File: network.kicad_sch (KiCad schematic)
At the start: 66 parts, among them J1 1840888-1, Q1 BSS138, Q2 BSS138, Q3 BSS138, U2 DP83867IRPAPR, Y1 ECS-2520MV-xxx-xx

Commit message: MDIX routing done
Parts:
- removed TP3: TestPoint, TestPoint:TestPoint_Pad_1.0x1.0mm, symbol Connector:TestPoint
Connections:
- net MD0_P: now reaches J1.2 (MD0+), U2.2 (TD_P_A)
- net MD0_N: now reaches J1.3 (MD0-), U2.3 (TD_M_A)
- net MD1_P: now reaches J1.4 (MD1+), U2.5 (TD_P_B)
- net MD1_N: now reaches J1.5 (MD1-), U2.6 (TD_M_B)
- net MD2_P: now reaches J1.6 (MD2+), U2.10 (TD_P_C)
- net MD2_N: now reaches J1.7 (MD2-), U2.11 (TD_M_C)
- net MD3_P: now reaches J1.8 (MD3+), U2.13 (TD_P_D)
- net MD3_N: now reaches J1.9 (MD3-), U2.14 (TD_M_D)
- no-connect marks 21 -> 22
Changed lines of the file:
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@@
+	)
+	(no_connect
+		(at 200.66 35.56)
 	)
 	(no_connect
@@
 		)
 	)
+	(label "MD2_P"
+		(at 218.44 58.42 0)
+		(effects
+			(font
+				(size 1.27 1.27)
+			)
+			(justify left bottom)
+		)
+	)
+	(label "MD2_N"
+		(at 218.44 60.96 0)
+		(effects
+			(font
+				(size 1.27 1.27)
+			)
+			(justify left bottom)
+		)
+	)
 	(label "LED2"
 		(at 262.89 148.59 180)
@@
 		)
 	)
+	(label "MD0_P"
+		(at 218.44 43.18 0)
+		(effects
+			(font
+				(size 1.27 1.27)
+			)
+			(justify left bottom)
+		)
+	)
 	(label "LED1"
 		(at 236.22 148.59 180)
@@
 		)
 	)
+	(label "MD0_N"
+		(at 218.44 45.72 0)
+		(effects
+			(font
+				(size 1.27 1.27)
+			)
+			(justify left bottom)
+		)
+	)
 	(label "3V3"
 		(at 20.32 106.68 180)
@@
 		)
 	)
+	(label "MD3_N"
+		(at 218.44 68.58 0)
+		(effects
+			(font
+				(size 1.27 1.27)
+			)
+			(justify left bottom)
+		)
+	)
 	(label "X_IN"
 		(at 198.12 121.92 0)
@@
 		)
 	)
+	(label "MD3_P"
+		(at 218.44 66.04 0)
+		(effects
+			(font
+				(size 1.27 1.27)
+			)
+			(justify left bottom)
+		)
+	)
 	(label "3V3"
 		(at 124.46 22.86 0)
+		(effects
+			(font
+				(size 1.27 1.27)
+			)
+			(justify left bottom)
+		)
+	)
+	(label "MD1_N"
+		(at 218.44 53.34 0)
+		(effects
+			(font
+				(size 1.27 1.27)
+			)
+			(justify left bottom)
+		)
+	)
+	(label "MD1_P"
+		(at 218.44 50.8 0)
 		(effects
 			(font
@@
 		(length 2.54)
 		(shape round)
-		(at 222.25 68.58 180)
-		(fields_autoplaced yes)
-		(effects
-			(font
-				(size 1.27 1.27)
-			)
-			(justify right bottom)
-		)
-		(property "Netclass" "MDI_DIFF_PAIR"
-			(at 222.9485 71.12 0)
-			(effects
-				(font
-					(size 1.27 1.27)
-				)
-				(justify left)
-			)
-		)
-		(property "Component Class" ""
-			(at -152.4 -1.27 0)
-			(effects
-				(font
-					(size 1.27 1.27)
-					(italic yes)
-				)
-			)
-		)
-	)
-	(netclass_flag ""
-		(length 2.54)
-		(shape round)
 		(at 101.6 83.82 180)
 		(fields_autoplaced yes)
@@
 				)
 			)
-		)
-	)
-	(symbol
-		(lib_id "Connector:TestPoint")
-		(at 200.66 35.56 270)
-		(unit 1)
-		(exclude_from_sim no)
-		(in_bom yes)
-		(on_board yes)
-		(dnp no)
-		(fields_autoplaced yes)
-		(property "Reference" "TP3"
-			(at 205.74 34.2899 90)
-			(effects
-				(font
-					(size 1.27 1.27)
-				)
-				(justify left)
-			)
-		)
-		(property "Value" "TestPoint"
-			(at 205.74 36.8299 90)
-			(effects
-				(font
-					(size 1.27 1.27)
-				)
-				(justify left)
-			)
-		)
-		(property "Footprint" "TestPoint:TestPoint_Pad_1.0x1.0mm"
-			(at 200.66 40.64 0)
-			(effects
-				(font
-					(size 1.27 1.27)
-				)
-				(hide yes)
-			)
-		)
-		(property "Datasheet" "~"
-			(at 200.66 40.64 0)
-			(effects
-				(font
-					(size 1.27 1.27)
-				)
-				(hide yes)
-			)
-		)
-		(property "Description" "test point"
-			(at 200.66 35.56 0)
-			(effects
-				(font
-					(size 1.27 1.27)
-				)
-				(hide yes)
-			)
-		)
-		(pin "1"
-		)
-		(instances
-			(project "pocketbeagle2 revA_241205"
-				(path "/82320ebb-b624-4fc9-8d5a-3bc164182d09/1a5f5f50-6711-4dc3-8e4f-1634784841ca"
-					(reference "TP3")
-					(unit 1)
-				)
-			)

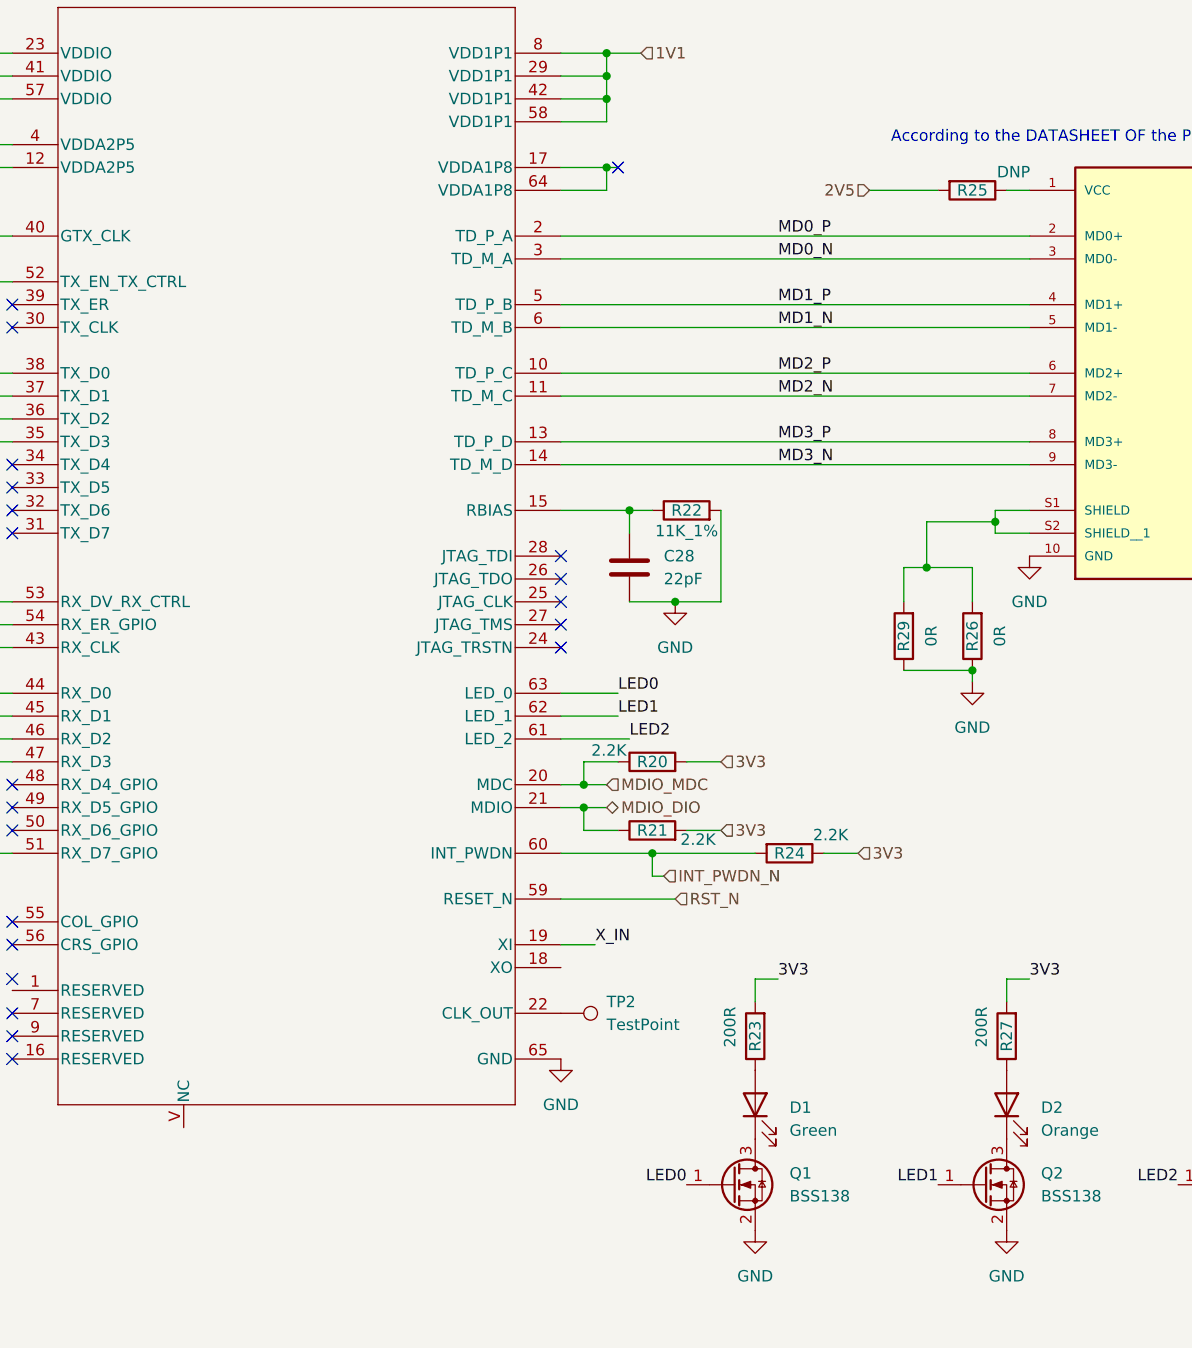
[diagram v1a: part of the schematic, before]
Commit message: Fully routed PCB, missing fligth time matching on the RGMII
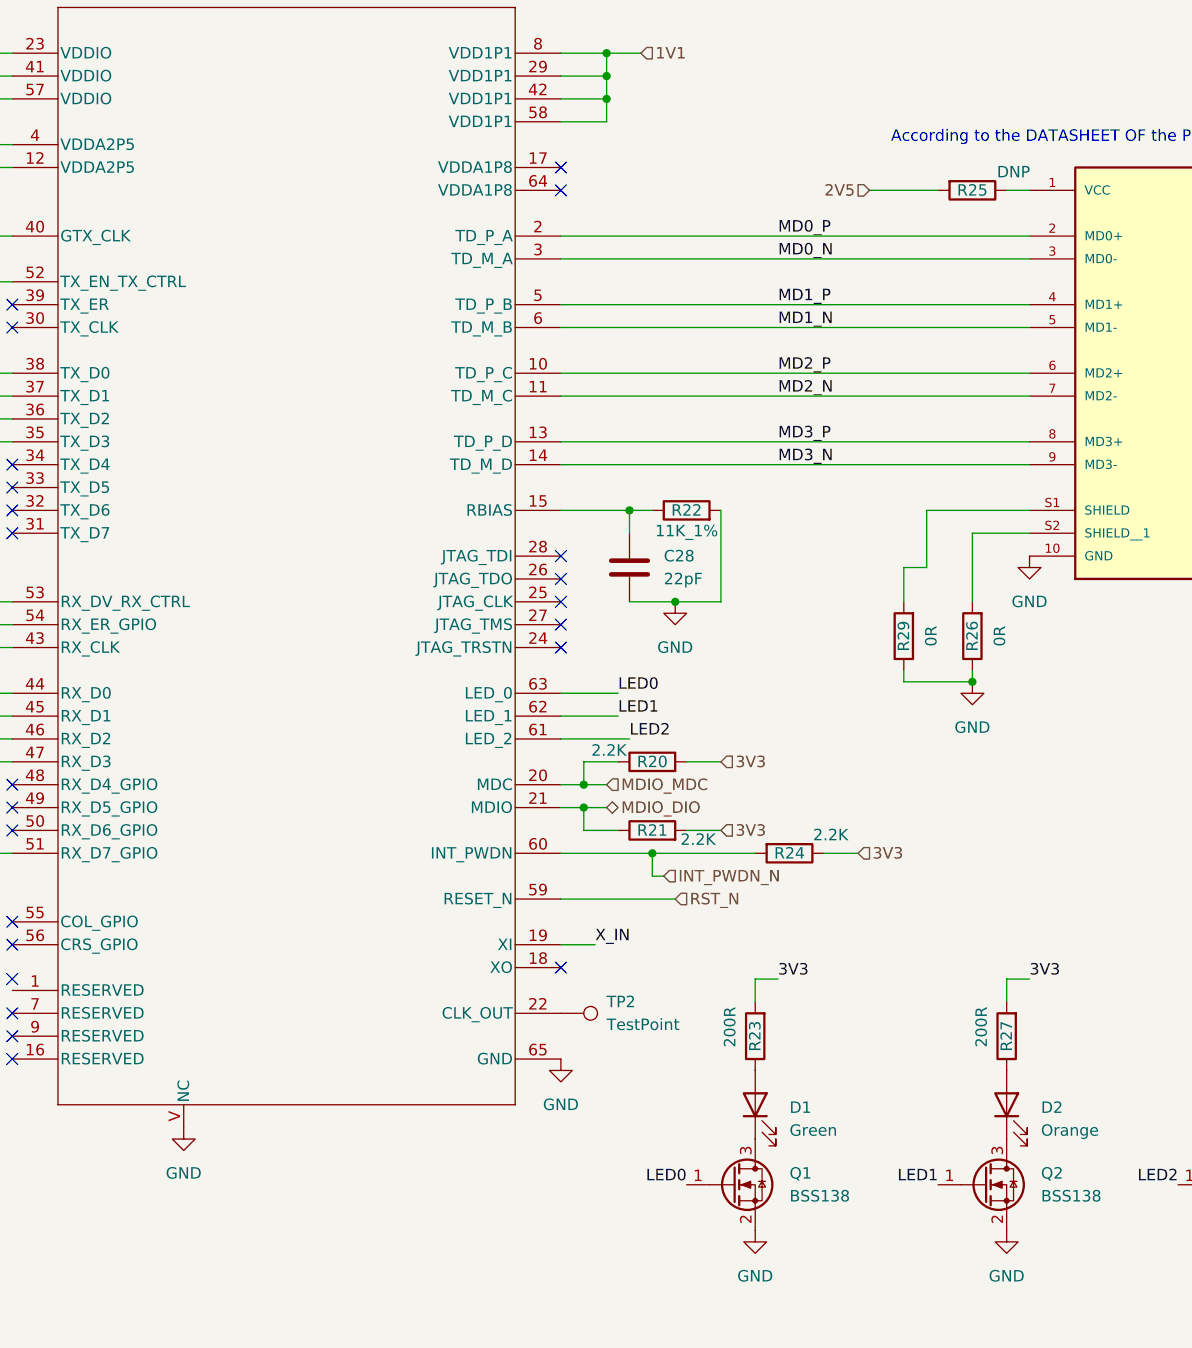
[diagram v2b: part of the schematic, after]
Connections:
- net GND: now also U2.V (NC)
- net at J1.S2 (SHIELD__1), R26.2: no longer J1.S1 (SHIELD), R29.2
- net at U2.17 (VDDA1P8): no longer U2.64 (VDDA1P8)
- new net: J1.S1 (SHIELD), R29.2
- no-connect marks 22 -> 24
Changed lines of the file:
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@@
 	)
 	(junction
+		(at 240.03 92.71)
+		(diameter 0)
+		(color 0 0 0 0)
+	)
+	(junction
 		(at 72.39 177.8)
 		(diameter 0)
@@
 	)
 	(junction
-		(at 240.03 91.44)
-		(diameter 0)
-		(color 0 0 0 0)
-	)
-	(junction
 		(at 110.49 171.45)
 		(diameter 0)
@@
 	)
 	(junction
-		(at 234.95 80.01)
-		(diameter 0)
-		(color 0 0 0 0)
-	)
-	(junction
 		(at 85.09 163.83)
 		(diameter 0)
@@
 	)
 	(junction
-		(at 199.39 35.56)
-		(diameter 0)
-		(color 0 0 0 0)
-	)
-	(junction
 		(at 72.39 149.86)
 		(diameter 0)
@@
 	)
 	(junction
-		(at 242.57 74.93)
-		(diameter 0)
-		(color 0 0 0 0)
-	)
-	(junction
 		(at 127 22.86)
 		(diameter 0)
@@
 	)
 	(no_connect
-		(at 133.35 73.66)
+		(at 194.31 124.46)
 	)
 	(no_connect
-		(at 200.66 35.56)
+		(at 133.35 73.66)
 	)
 	(no_connect
@@
 	)
 	(no_connect
+		(at 194.31 35.56)
+	)
+	(no_connect
 		(at 194.31 88.9)
 	)
@@
 	)
 	(no_connect
+		(at 194.31 38.1)
+	)
+	(no_connect
 		(at 133.35 125.73)
 	)
@@
 	(wire
 		(pts
-			(xy 234.95 80.01) (xy 240.03 80.01)
+			(xy 234.95 80.01) (xy 232.41 80.01)
 		)
 		(stroke
@@
 	(wire
 		(pts
-			(xy 242.57 76.2) (xy 246.38 76.2)
+			(xy 232.41 91.44) (xy 232.41 92.71)
 		)
 		(stroke
@@
 	(wire
 		(pts
-			(xy 242.57 76.2) (xy 242.57 74.93)
-		)
-		(stroke
-			(width 0)
-			(type default)
-		)
-	)
-	(wire
-		(pts
 			(xy 59.69 163.83) (xy 72.39 163.83)
 		)
@@
 	(wire
 		(pts
-			(xy 194.31 38.1) (xy 199.39 38.1)
-		)
-		(stroke
-			(width 0)
-			(type default)
-		)
-	)
-	(wire
-		(pts
 			(xy 97.79 93.98) (xy 120.65 93.98)
 		)
@@
 	(wire
 		(pts
-			(xy 234.95 80.01) (xy 234.95 74.93)
+			(xy 234.95 73.66) (xy 246.38 73.66)
+		)
+		(stroke
+			(width 0)
+			(type default)
+		)
+	)
+	(wire
+		(pts
+			(xy 234.95 73.66) (xy 234.95 80.01)
 		)
 		(stroke
@@
 	(wire
 		(pts
-			(xy 199.39 38.1) (xy 199.39 35.56)
-		)
-		(stroke
-			(width 0)
-			(type default)
-		)
-	)
-	(wire
-		(pts
 			(xy 199.39 30.48) (xy 199.39 27.94)
 		)
@@
 	(wire
 		(pts
-			(xy 240.03 83.82) (xy 240.03 80.01)
-		)
-		(stroke
-			(width 0)
-			(type default)
-		)
-	)
-	(wire
-		(pts
 			(xy 97.79 99.06) (xy 120.65 99.06)
 		)
@@
 	(wire
 		(pts
-			(xy 242.57 74.93) (xy 242.57 73.66)
-		)
-		(stroke
-			(width 0)
-			(type default)
-		)
-	)
-	(wire
-		(pts
-			(xy 199.39 35.56) (xy 200.66 35.56)
+			(xy 240.03 91.44) (xy 240.03 92.71)
 		)
 		(stroke
@@
 	(wire
 		(pts
-			(xy 240.03 91.44) (xy 240.03 92.71)
+			(xy 97.79 101.6) (xy 120.65 101.6)
 		)
 		(stroke
@@
 	(wire
 		(pts
-			(xy 97.79 101.6) (xy 120.65 101.6)
+			(xy 196.85 106.68) (xy 199.39 106.68)
 		)
 		(stroke
@@
 	(wire
 		(pts
-			(xy 196.85 106.68) (xy 199.39 106.68)
+			(xy 240.03 76.2) (xy 240.03 83.82)
 		)
 		(stroke
@@
 	(wire
 		(pts
-			(xy 194.31 35.56) (xy 199.39 35.56)
+			(xy 232.41 92.71) (xy 240.03 92.71)
 		)
 		(stroke
@@
 	(wire
 		(pts
-			(xy 234.95 74.93) (xy 242.57 74.93)
+			(xy 246.38 76.2) (xy 240.03 76.2)
 		)
 		(stroke
@@
 	(wire
 		(pts
-			(xy 232.41 91.44) (xy 240.03 91.44)
-		)
-		(stroke
-			(width 0)
-			(type default)
-		)
-	)
-	(wire
-		(pts
 			(xy 127 33.02) (xy 133.35 33.02)
 		)
@@
 	(wire
 		(pts
-			(xy 242.57 73.66) (xy 246.38 73.66)
-		)
-		(stroke
-			(width 0)
-			(type default)
-		)
-	)
-	(wire
-		(pts
-			(xy 232.41 80.01) (xy 234.95 80.01)
-		)
-		(stroke
-			(width 0)
-			(type default)
-		)
-	)
-	(wire
-		(pts
 			(xy 26.67 82.55) (xy 26.67 83.82)
 		)
@@
 					(unit 1)
 				)
+			)
+		)
+	)
+	(symbol
+		(lib_id "power:GND")
+		(at 152.4 142.24 0)
+		(unit 1)
+		(exclude_from_sim no)
+		(in_bom yes)
+		(on_board yes)
+		(dnp no)
+		(fields_autoplaced yes)
+		(property "Reference" "#PWR028"
+			(at 152.4 148.59 0)
+			(effects
+				(font
+					(size 1.27 1.27)
+				)
+				(hide yes)
+			)
+		)
+		(property "Value" "GND"
+			(at 152.4 147.32 0)
+			(effects
+				(font
+					(size 1.27 1.27)
+				)
+			)
+		)
+		(property "Footprint" ""
+			(at 152.4 142.24 0)
+			(effects
+				(font
+					(size 1.27 1.27)
+				)
+				(hide yes)
+			)
+		)
+		(property "Datasheet" ""
+			(at 152.4 142.24 0)
+			(effects
+				(font
+					(size 1.27 1.27)
+				)
+				(hide yes)
+			)
+		)
+		(property "Description" "Power symbol creates a global label with name \"GND\" , ground"
+			(at 152.4 142.24 0)
+			(effects
+				(font
+					(size 1.27 1.27)
+				)
+				(hide yes)
+			)
+		)
+		(pin "1"
+		)
+		(instances
+			(project "pocketbeagle2 revA_241205"
+				(path "/82320ebb-b624-4fc9-8d5a-3bc164182d09/1a5f5f50-6711-4dc3-8e4f-1634784841ca"
+					(reference "#PWR028")
+					(unit 1)
+				)
